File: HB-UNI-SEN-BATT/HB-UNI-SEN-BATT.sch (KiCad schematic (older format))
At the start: 20 parts, among them J0 BATT, J1 I2C_1, J2 I2C_2, J3 A0, J4 A1, J5 A2, J6 A3, J7 PROG, SW1 CONFIG_BUTTON, U1 ArduinoProMini, U2 CC1101

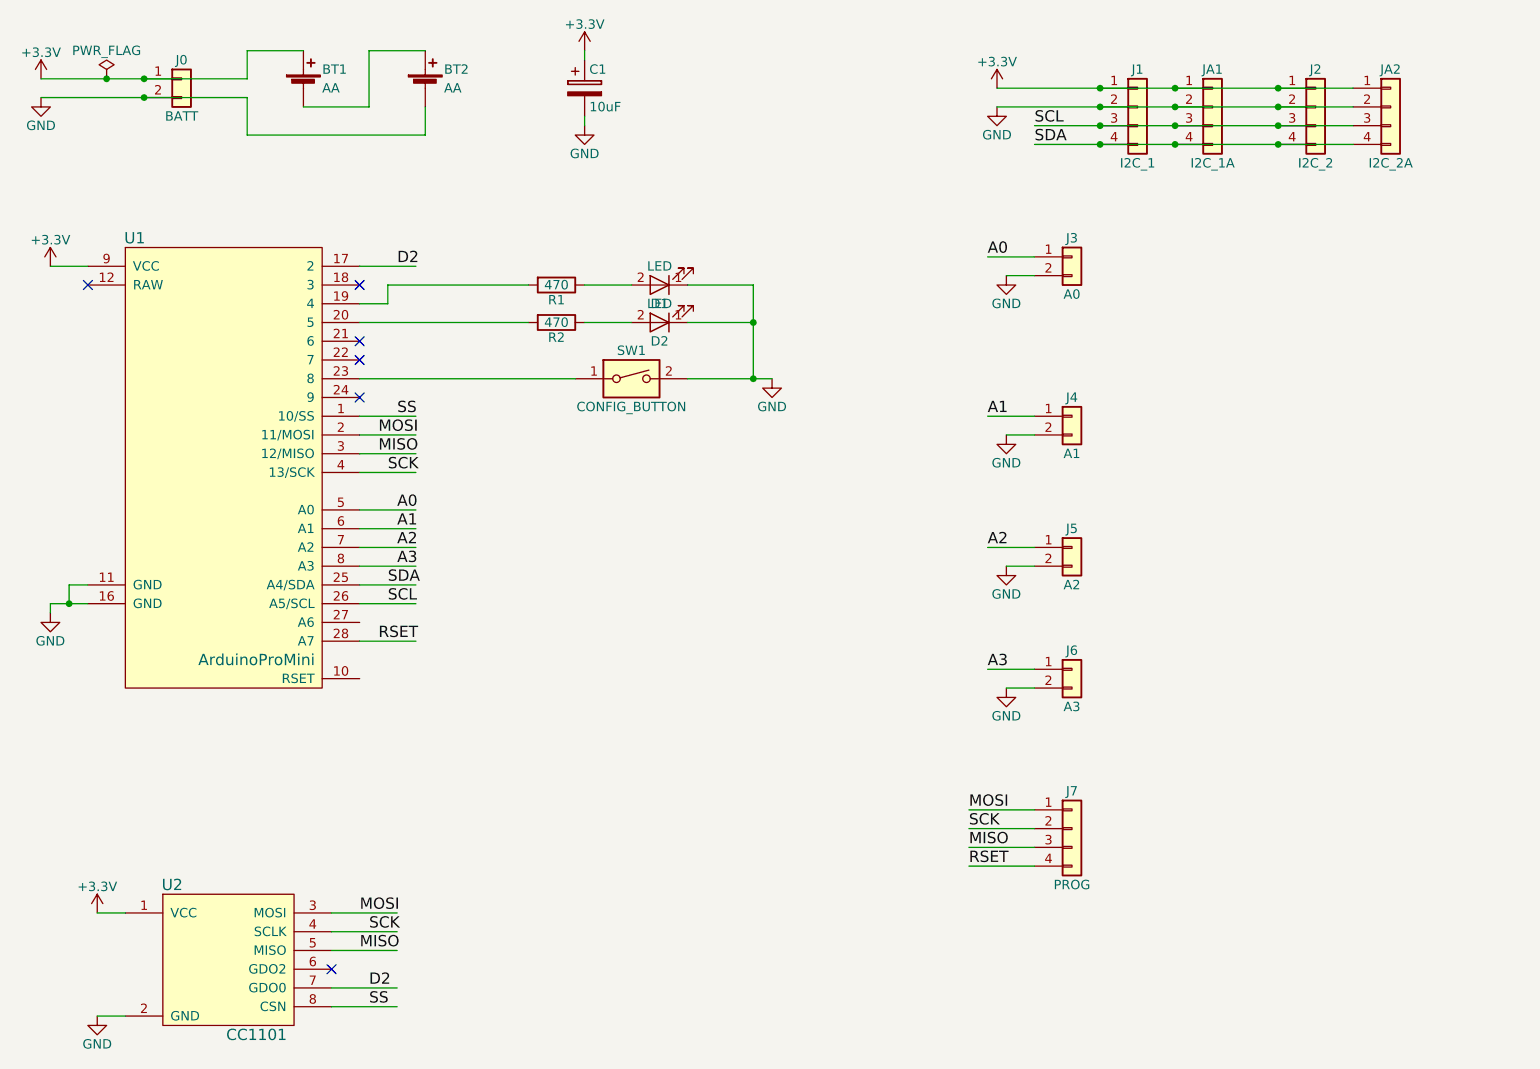
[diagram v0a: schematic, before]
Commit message: Added reverse polarity protection
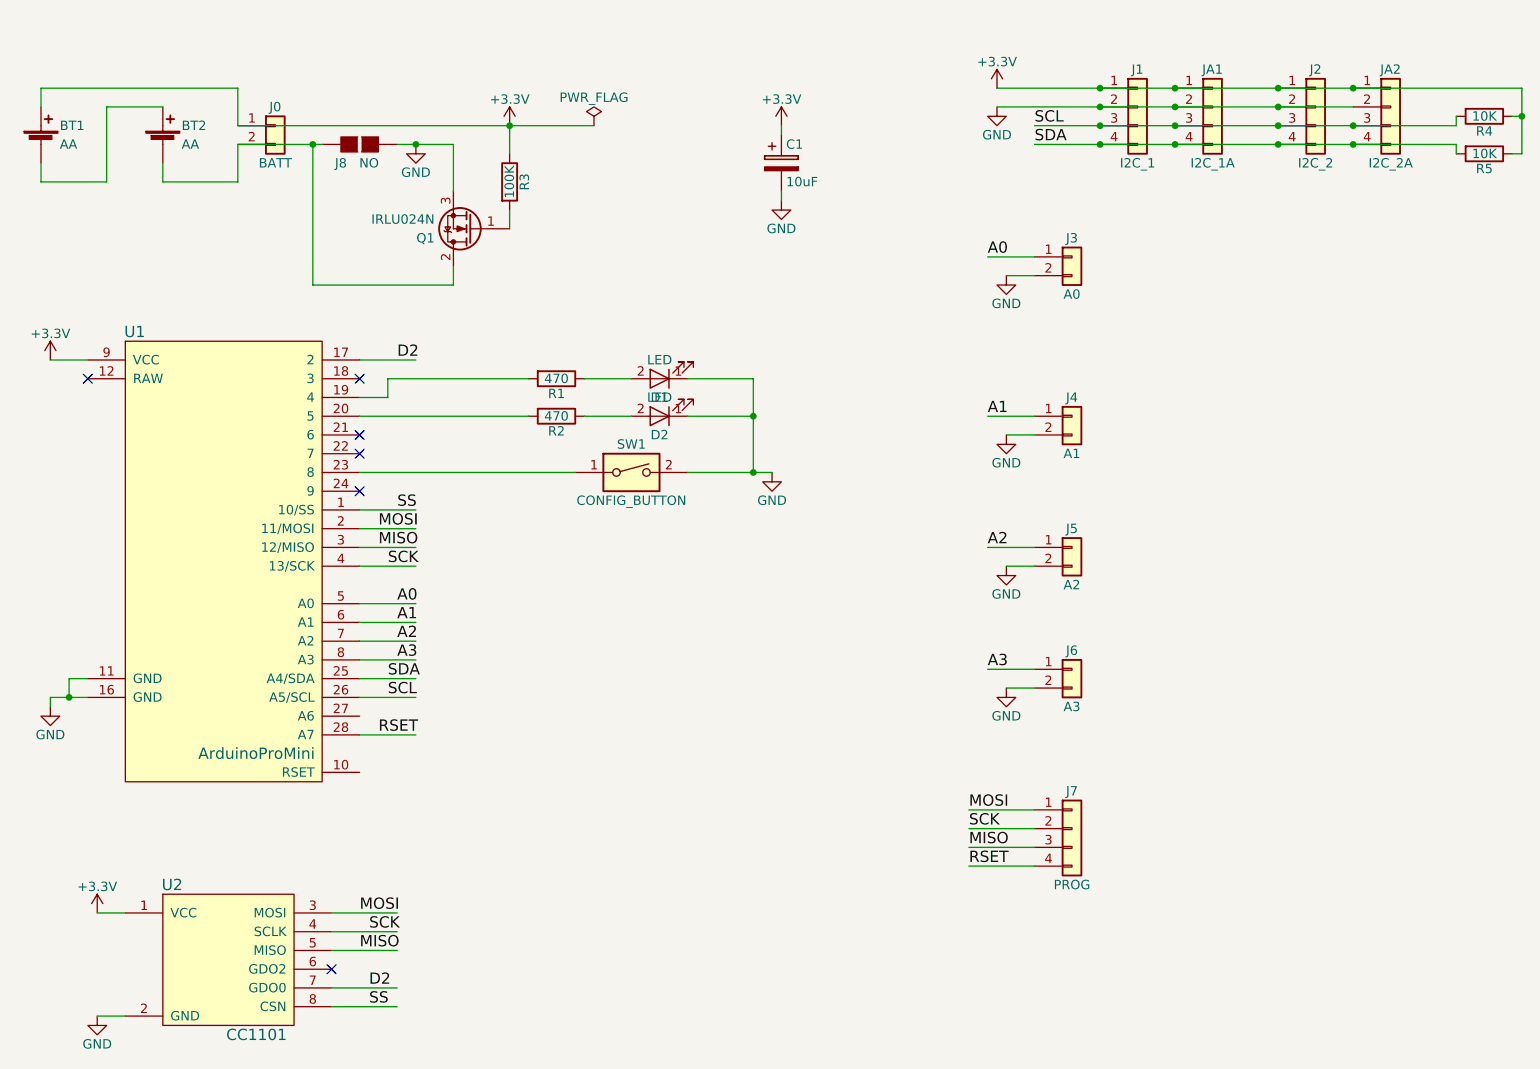
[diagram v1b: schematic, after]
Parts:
- added J8: NO, Connectors:GS2, symbol GS2
- added Q1: IRLU024N, TO_SOT_Packages_THT:TO-251_IPAK_Vertical, symbol Q_NMOS_GDS
- added R3: 100K, Resistors_THT:R_Axial_DIN0207_L6.3mm_D2.5mm_P2.54mm_Vertical, symbol R
- added R4, R5: 10K, Resistors_THT:R_Axial_DIN0207_L6.3mm_D2.5mm_P2.54mm_Vertical, symbol R
- R1, R2: footprint Resistors_THT:R_Axial_DIN0207_L6.3mm_D2.5mm_P10.16mm_Horizontal -> Resistors_THT:R_Axial_DIN0207_L6.3mm_D2.5mm_P2.54mm_Vertical
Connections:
- wire segments 63 -> 77
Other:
- moved on the sheet: BT1, BT2, C1, D1, D2, J0, R1, R2, SW1, U1

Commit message: Added new PCB HB-UNI-644, removed unfinished HB-UNI-SEN-O
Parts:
- U2: symbol CC1101 -> CC1101-RESCUE-HB-UNI-SEN-BATT
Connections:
- no-connect marks 6 -> 8
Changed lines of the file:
@@
 EESchema Schematic File Version 2
+LIBS:HB-UNI-SEN-BATT-rescue
 LIBS:power
 LIBS:device
@@
 Sheet 1 1
 Title "HB-UNI-SEN-BATT"
-Date "2018-05-03"
-Rev "1.5"
+Date "2018-05-11"
+Rev "1.6"
 Comp "Alexander Reinert"
 Comment1 ""
@@
 $EndComp
 $Comp
-L CC1101 U2
+L CC1101-RESCUE-HB-UNI-SEN-BATT U2
 U 1 1 5AC3AFA1
 P 1650 5900
@@
 F 3 "" H 4800 3000 50  0001 C CNN
 	1    4800 3000
-	1    0    0    -1
-$EndComp
-$Comp
-L ArduinoProMini U1
-U 1 1 5ACA0010
-P 1900 3600
-F 0 "U1" H 1400 4950 60  0000 C CNN
-F 1 "ArduinoProMini" H 2050 2700 60  0000 C CNN
-F 2 "Homebrew:ArduinoProMini" H 1900 3500 60  0001 C CNN
-F 3 "" H 1900 3500 60  0001 C CNN
-	1    1900 3600
 	1    0    0    -1
 $EndComp
@@
 Text Label 2750 4200 0    60   ~ 0
 SCL
-Text Label 2700 4400 0    60   ~ 0
+Text Label 2700 4600 0    60   ~ 0
 RSET
 Text Label 2600 5350 0    60   ~ 0
@@
 	2600 4200 2900 4200
 Wire Wire Line
-	2600 4400 2900 4400
-Wire Wire Line
 	2750 2600 2750 2500
 Wire Wire Line
@@
 Connection ~ 2350 1250
 Connection ~ 2900 1250
+$Comp
+L ArduinoProMini U1
+U 1 1 5AF60D3E
+P 1900 3600
+F 0 "U1" H 1400 4950 60  0000 C CNN
+F 1 "ArduinoProMini" H 2050 2450 60  0000 C CNN
+F 2 "Homebrew:ArduinoProMini" H 1900 3500 60  0001 C CNN
+F 3 "" H 1900 3500 60  0001 C CNN
+	1    1900 3600
+	1    0    0    -1
+$EndComp
+Wire Wire Line
+	2600 4600 2900 4600
+NoConn ~ 2600 4400
+NoConn ~ 2600 4300
 $EndSCHEMATC

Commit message: * Switched to Kicad 5 * Added HB-UNI-644-S4-A4 addon Board
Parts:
- BT1, BT2: symbol Battery_Cell -> Device:Battery_Cell
- C1: symbol CP -> Device:CP
- D1, D2: symbol LED -> Device:LED
- J0, J3, J4, J5, J6: symbol Conn_01x02 -> conn:Conn_01x02
- J1, J2, J7, JA1, JA2: symbol Conn_01x04 -> conn:Conn_01x04
- J8: symbol GS2 -> conn:GS2
- Q1: symbol Q_NMOS_GDS -> Device:Q_NMOS_GDS
- R1, R2, R3, R4, R5: symbol R -> Device:R
- SW1: symbol SW_DIP_x01 -> switches:SW_DIP_x01
- U1: symbol ArduinoProMini -> Homebrew:ArduinoProMini
- U2: symbol CC1101-RESCUE-HB-UNI-SEN-BATT -> HB-UNI-SEN-BATT-rescue:CC1101-RESCUE-HB-UNI-SEN-BATT
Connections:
- wire segments 77 -> 99
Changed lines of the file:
@@
-EESchema Schematic File Version 2
-LIBS:HB-UNI-SEN-BATT-rescue
-LIBS:power
-LIBS:device
-LIBS:switches
-LIBS:relays
-LIBS:motors
-LIBS:transistors
-LIBS:conn
-LIBS:linear
-LIBS:regul
-LIBS:74xx
-LIBS:cmos4000
-LIBS:adc-dac
-LIBS:memory
-LIBS:xilinx
-LIBS:microcontrollers
-LIBS:dsp
-LIBS:microchip
-LIBS:analog_switches
-LIBS:motorola
-LIBS:texas
-LIBS:intel
-LIBS:audio
-LIBS:interface
-LIBS:digital-audio
-LIBS:philips
-LIBS:display
-LIBS:cypress
-LIBS:siliconi
-LIBS:opto
-LIBS:atmel
-LIBS:contrib
-LIBS:valves
-LIBS:Homebrew
+EESchema Schematic File Version 4
 LIBS:HB-UNI-SEN-BATT-cache
-EELAYER 25 0
+EELAYER 26 0
 EELAYER END
 $Descr A4 11693 8268
@@
 $EndDescr
 $Comp
-L Conn_01x04 J1
+L conn:Conn_01x04 J1
 U 1 1 5ABE0D25
 P 6750 1050
@@
 $EndComp
 $Comp
-L Conn_01x04 J2
+L conn:Conn_01x04 J2
 U 1 1 5ABE0DC1
 P 7700 1050
@@
 $EndComp
 $Comp
-L SW_DIP_x01 SW1
+L switches:SW_DIP_x01 SW1
 U 1 1 5ABE0E28
 P 4050 3000
@@
 $EndComp
 $Comp
-L LED D1
+L Device:LED D1
 U 1 1 5ABE1195
 P 4200 2500
@@
 $EndComp
 $Comp
-L +3.3V #PWR01
+L power:+3.3V #PWR01
 U 1 1 5ABE128D
 P 950 2400
@@
 $EndComp
 $Comp
-L Conn_01x02 J5
+L conn:Conn_01x02 J5
 U 1 1 5ABE1F9E
 P 6400 3400
@@
 $EndComp
 $Comp
-L Conn_01x02 J6
+L conn:Conn_01x02 J6
 U 1 1 5ABE2007
 P 6400 4050
@@
 $EndComp
 $Comp
-L R R1
+L Device:R R1
 U 1 1 5ABE25C7
 P 3650 2500
@@
 $EndComp
 $Comp
-L Conn_01x02 J0
+L conn:Conn_01x02 J0
 U 1 1 5ABE2E32
 P 2150 1150
@@
 $EndComp
 $Comp
-L CC1101-RESCUE-HB-UNI-SEN-BATT U2
+L HB-UNI-SEN-BATT-rescue:CC1101-RESCUE-HB-UNI-SEN-BATT U2
 U 1 1 5AC3AFA1
 P 1650 5900
@@
 $EndComp
 $Comp
-L Conn_01x04 J7
+L conn:Conn_01x04 J7
 U 1 1 5AC3B268
 P 6400 4900
@@
 $EndComp
 $Comp
-L +3.3V #PWR02
+L power:+3.3V #PWR02
 U 1 1 5AC7DE60
 P 6000 950
@@
 $EndComp
 $Comp
-L GND #PWR03
+L power:GND #PWR03
 U 1 1 5AC7DE98
 P 6000 1050
@@
 $EndComp
 $Comp
-L +3.3V #PWR04
+L power:+3.3V #PWR04
 U 1 1 5AC7EBE5
 P 3400 1150
@@
 $EndComp
 $Comp
-L GND #PWR05
+L power:GND #PWR05
 U 1 1 5AC7ECC2
 P 2900 1250
@@
 $EndComp
 $Comp
-L GND #PWR06
+L power:GND #PWR06
 U 1 1 5AC7F222
 P 6050 1950
@@
 $EndComp
 $Comp
-L +3.3V #PWR07
+L power:+3.3V #PWR07
 U 1 1 5AC7F4EE
 P 1200 5350
@@
 $EndComp
 $Comp
-L GND #PWR08
+L power:GND #PWR08
 U 1 1 5AC7FA89
 P 1200 5900
@@
 $EndComp
 $Comp
-L GND #PWR09
+L power:GND #PWR09
 U 1 1 5AC7FD3C
 P 950 4250
@@
 $EndComp
 $Comp
-L GND #PWR010
+L power:GND #PWR010
 U 1 1 5AC8103C
 P 6050 2800
@@
 $EndComp
 $Comp
-L GND #PWR011
+L power:GND #PWR011
 U 1 1 5AC81356
 P 6050 3500
@@
 $EndComp
 $Comp
-L GND #PWR012
+L power:GND #PWR012
 U 1 1 5AC81860
 P 6050 4150
@@
 $EndComp
 $Comp
-L GND #PWR013
+L power:GND #PWR013
 U 1 1 5AC84E05
 P 4800 3000
@@
 $EndComp
 $Comp
-L PWR_FLAG #FLG014
+L power:PWR_FLAG #FLG014
 U 1 1 5ACA03CA
 P 3850 1150
@@
 SCL
 $Comp
-L Battery_Cell BT1
+L Device:Battery_Cell BT1
 U 1 1 5ACCD42F
 P 900 1250
@@
 $EndComp
 $Comp
-L Battery_Cell BT2
+L Device:Battery_Cell BT2
 U 1 1 5ACCD555
 P 1550 1250
@@
 $EndComp
 $Comp
-L Conn_01x04 JA1
+L conn:Conn_01x04 JA1
 U 1 1 5AD9EB60
 P 7150 1050
@@
 $EndComp
 $Comp
-L Conn_01x04 JA2
+L conn:Conn_01x04 JA2
 U 1 1 5AD9EE00
 P 8100 1050
@@
 $EndComp
 $Comp
-L Conn_01x02 J4
+L conn:Conn_01x02 J4
 U 1 1 5AD9F8DF
 P 6400 2700
@@
 $EndComp
 $Comp
-L Conn_01x02 J3
+L conn:Conn_01x02 J3
 U 1 1 5AD9FA61
 P 6400 1850
@@
 $EndComp
 $Comp
-L R R2
+L Device:R R2
 U 1 1 5AD9FCAF
 P 3650 2700
@@
 $EndComp
 $Comp
-L LED D2
+L Device:LED D2
 U 1 1 5AD9FCFD
 P 4200 2700
@@
 NoConn ~ 2600 2800
 $Comp
-L +3.3V #PWR015
+L power:+3.3V #PWR015
 U 1 1 5ADA3963
 P 4850 1150
@@
 $EndComp
 $Comp
-L GND #PWR016
+L power:GND #PWR016
 U 1 1 5ADA39CD
 P 4850 1550
@@
 $EndComp
 $Comp
-L CP C1
+L Device:CP C1
 U 1 1 5ADA3A00
 P 4850 1350
@@
 	1200 5900 1350 5900
 Wire Wire Line
-	950  4200 1150 4200
+	950  4200 1050 4200
 Wire Wire Line
 	950  4250 950  4200
@@
 	4350 2500 4700 2500
 Wire Wire Line
-	4700 2500 4700 3000
-Wire Wire Line
-	4350 3000 4800 3000
+	4700 2500 4700 2700
+Wire Wire Line
+	4350 3000 4700 3000
 Connection ~ 4700 3000
 Wire Wire Line
@@
 	1250 1050 1550 1050
 Wire Wire Line
-	6000 950  8800 950
+	6000 950  6550 950
 Connection ~ 7500 950
 Connection ~ 6950 950
 Wire Wire Line
-	6000 1050 7900 1050
+	6000 1050 6550 1050
 Connection ~ 6950 1050
 Connection ~ 7500 1050
 Wire Wire Line
-	6200 1150 8450 1150
+	6200 1150 6550 1150
 Connection ~ 6950 1150
 Connection ~ 7500 1150
@@
 Connection ~ 4700 2700
 Wire Wire Line
-	6200 1250 8450 1250
+	6200 1250 6550 1250
 Wire Wire Line
 	6050 1950 6200 1950
@@
 	1550 1450 1950 1450
 Wire Wire Line
-	1950 1150 3850 1150
-Wire Wire Line
-	1950 1250 2400 1250
+	1950 1150 3400 1150
+Wire Wire Line
+	1950 1250 2350 1250
 Wire Wire Line
 	2350 1250 2350 2000
 Connection ~ 3400 1150
 $Comp
-L R R4
+L Device:R R4
 U 1 1 5AE847F0
 P 8600 1100
@@
 $EndComp
 $Comp
-L R R5
+L Device:R R5
 U 1 1 5AE848BD
 P 8600 1300
@@
 Connection ~ 7900 1150
 Wire Wire Line
-	8800 950  8800 1300
+	8800 950  8800 1100
 Wire Wire Line
 	8800 1300 8750 1300
@@
 Connection ~ 8800 1100
 $Comp
-L Q_NMOS_GDS Q1
+L Device:Q_NMOS_GDS Q1
 U 1 1 5AE8D841
 P 3200 1700
@@
 	2350 2000 3100 2000
 $Comp
-L R R3
+L Device:R R3
 U 1 1 5AE8DE1E
 P 3400 1450
@@
 	3400 1300 3400 1150
 Wire Wire Line
-	2800 1250 3100 1250
+	2800 1250 2900 1250
 Wire Wire Line
 	3100 1250 3100 1500
 $Comp
-L GS2 J8
+L conn:GS2 J8
 U 1 1 5AEB2F42
 P 2600 1250
@@
 Connection ~ 2900 1250
 $Comp
-L ArduinoProMini U1
+L Homebrew:ArduinoProMini U1
 U 1 1 5AF60D3E
 P 1900 3600
@@
 NoConn ~ 2600 4400
 NoConn ~ 2600 4300
+Wire Wire Line
+	6550 950  6950 950
+Wire Wire Line
+	6550 1050 6950 1050
+Wire Wire Line
+	6550 1250 6950 1250
+Wire Wire Line
+	6550 1150 6950 1150
+Wire Wire Line
+	1050 4200 1150 4200
+Wire Wire Line
+	4700 3000 4800 3000
+Wire Wire Line
+	7500 950  7900 950
+Wire Wire Line
+	6950 950  7500 950
+Wire Wire Line
+	6950 1050 7500 1050
+Wire Wire Line
+	7500 1050 7900 1050
+Wire Wire Line
+	6950 1150 7500 1150
+Wire Wire Line
+	7500 1150 7900 1150
+Wire Wire Line
+	6950 1250 7500 1250
+Wire Wire Line
+	7500 1250 7900 1250
+Wire Wire Line
+	4700 2700 4700 3000
+Wire Wire Line
+	3400 1150 3850 1150
+Wire Wire Line
+	7900 1250 8450 1250
+Wire Wire Line
+	7900 1150 8450 1150
+Wire Wire Line
+	7900 950  8800 950
+Wire Wire Line
+	8800 1100 8800 1300
+Wire Wire Line
+	2350 1250 2400 1250
+Wire Wire Line
+	2900 1250 3100 1250
 $EndSCHEMATC
